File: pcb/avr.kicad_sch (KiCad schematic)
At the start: 17 parts, among them J11 PEN, J14 ATMegaSpare, J16 ATUART, J18 Reset ext, J4 AVR ISP, J6 Enable load, SW2 Reset btn, U22 ATmega128L-8A, Y3 16MHz

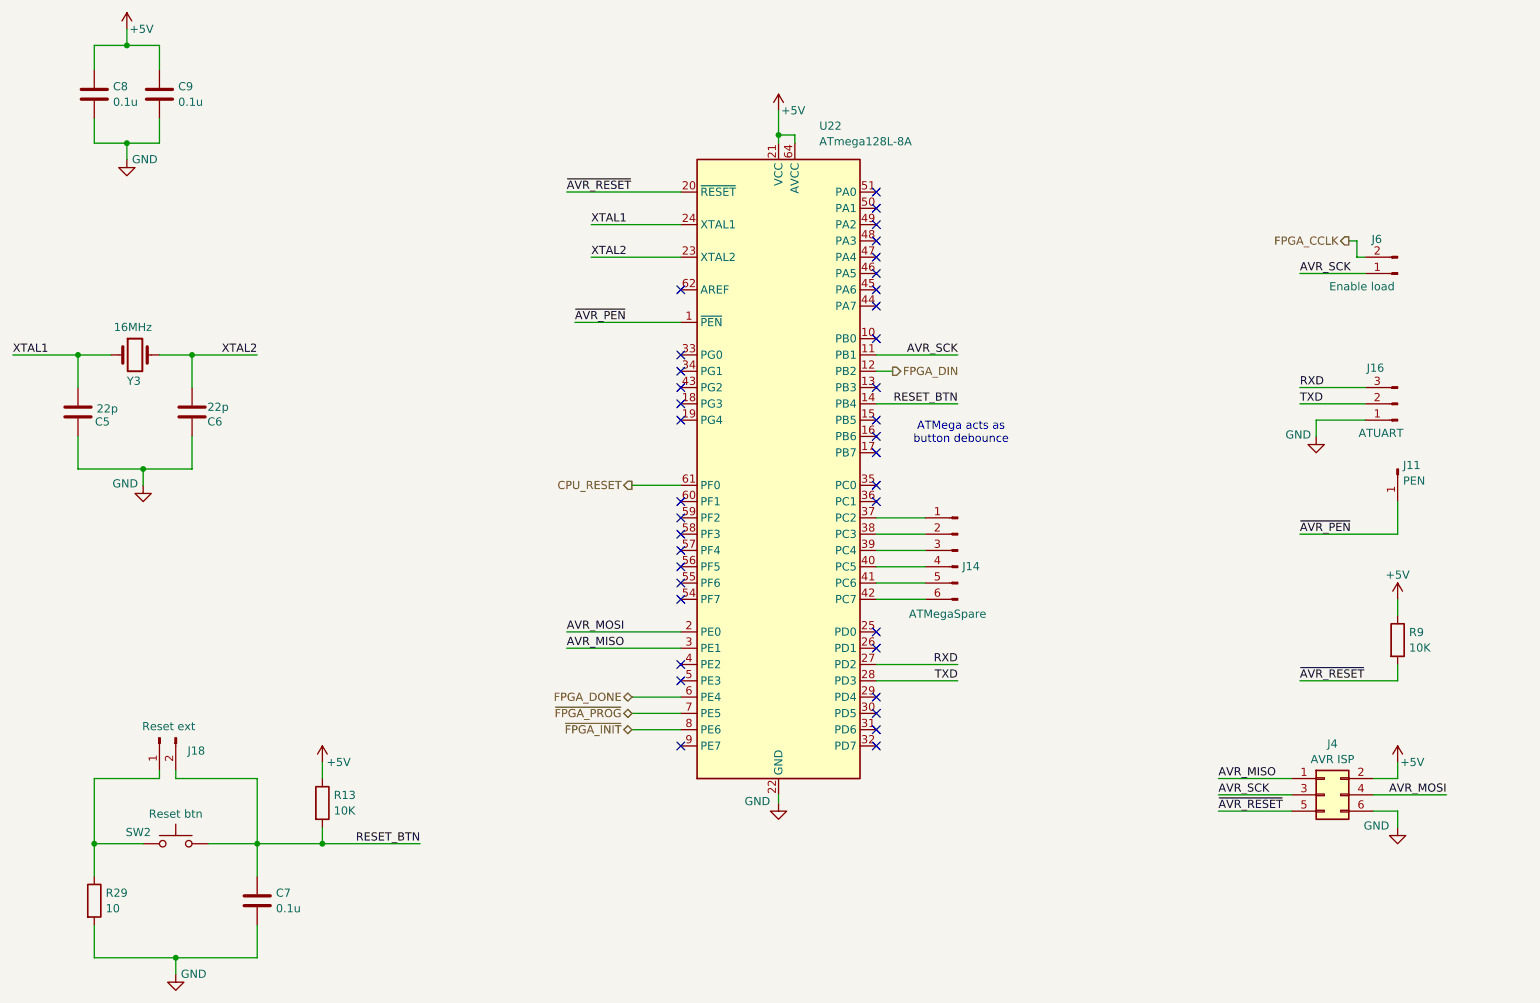
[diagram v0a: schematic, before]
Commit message: reshuffling atmega IO for better PCB routing
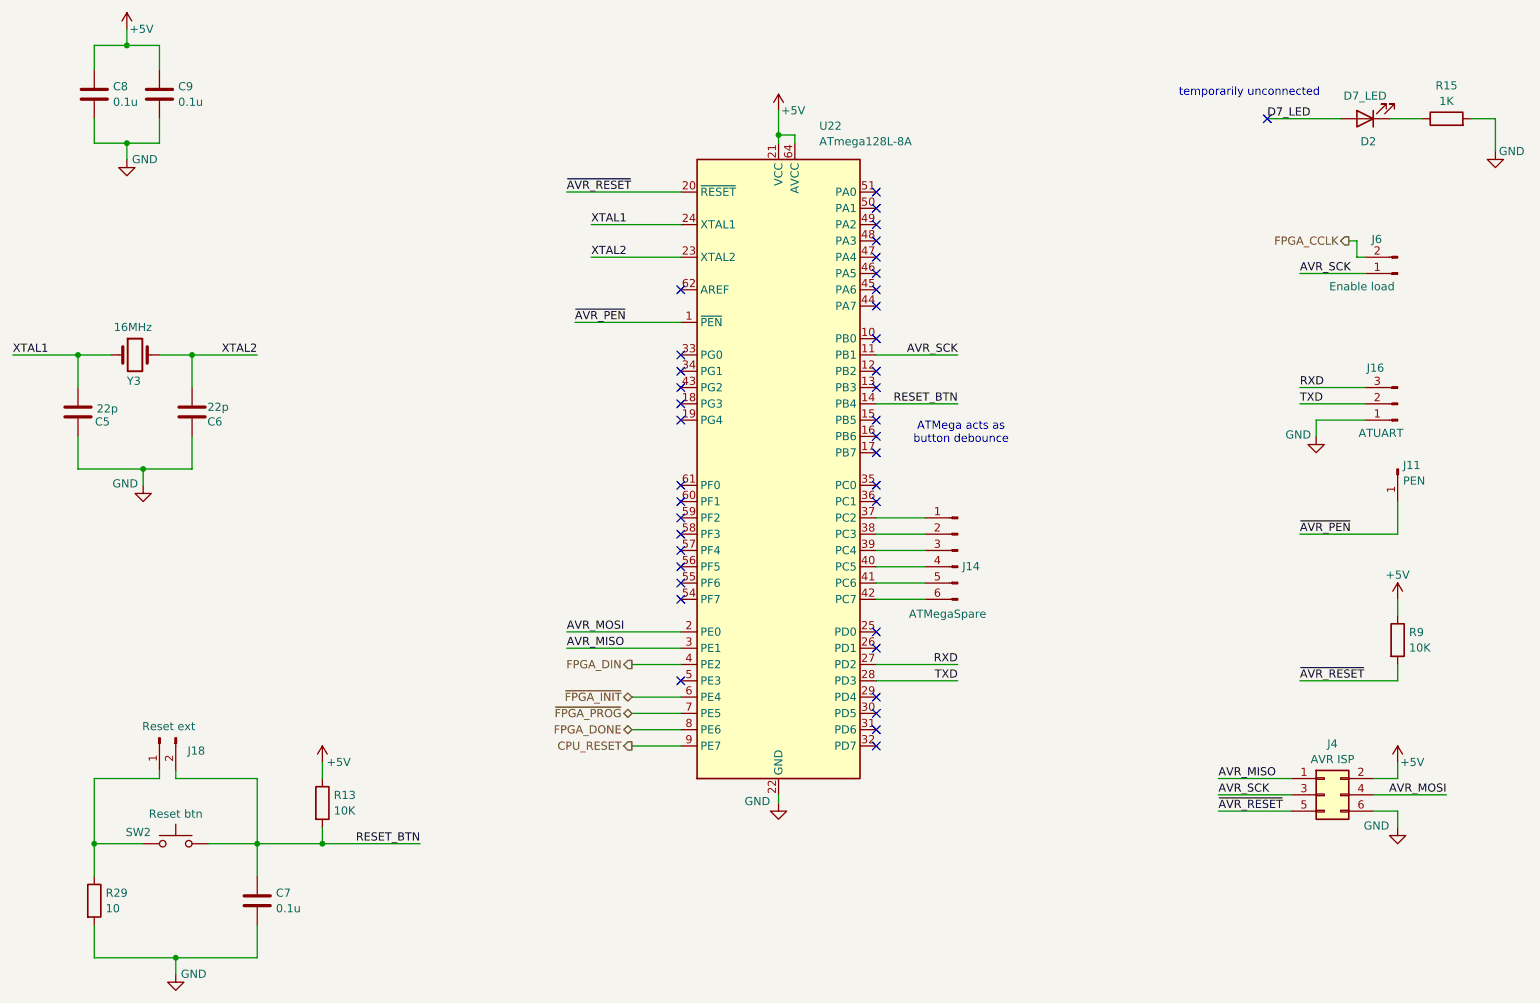
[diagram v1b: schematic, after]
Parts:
- added D2: D7_LED, LED_THT:LED_D4.0mm, symbol Device:LED
- added R15: 1K, Resistor_SMD:R_0805_2012Metric_Pad1.20x1.40mm_HandSolder, symbol Device:R
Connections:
- net CPU_RESET: now also U22.9 (PE7); no longer U22.61 (PF0)
- net FPGA_DIN: now also U22.4 (PE2); no longer U22.12 (PB2)
- net FPGA_DONE: now also U22.8 (PE6); no longer U22.6 (PE4)
- net GND: now also R15.2
- net ~{FPGA_INIT}: now also U22.6 (PE4); no longer U22.8 (PE6)
- new net: D2.1 (K), R15.1
- new net D7_LED: D2.2 (A)
- no-connect marks 37 -> 38
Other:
- note added: "temporarily unconnected"

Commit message: AVR diagram CMOS header, FPGA_DIN back to pin 12, CPU_RESET pin 5, simplified RESET_BTN circuit (pullup and debounce is inside AVR already)
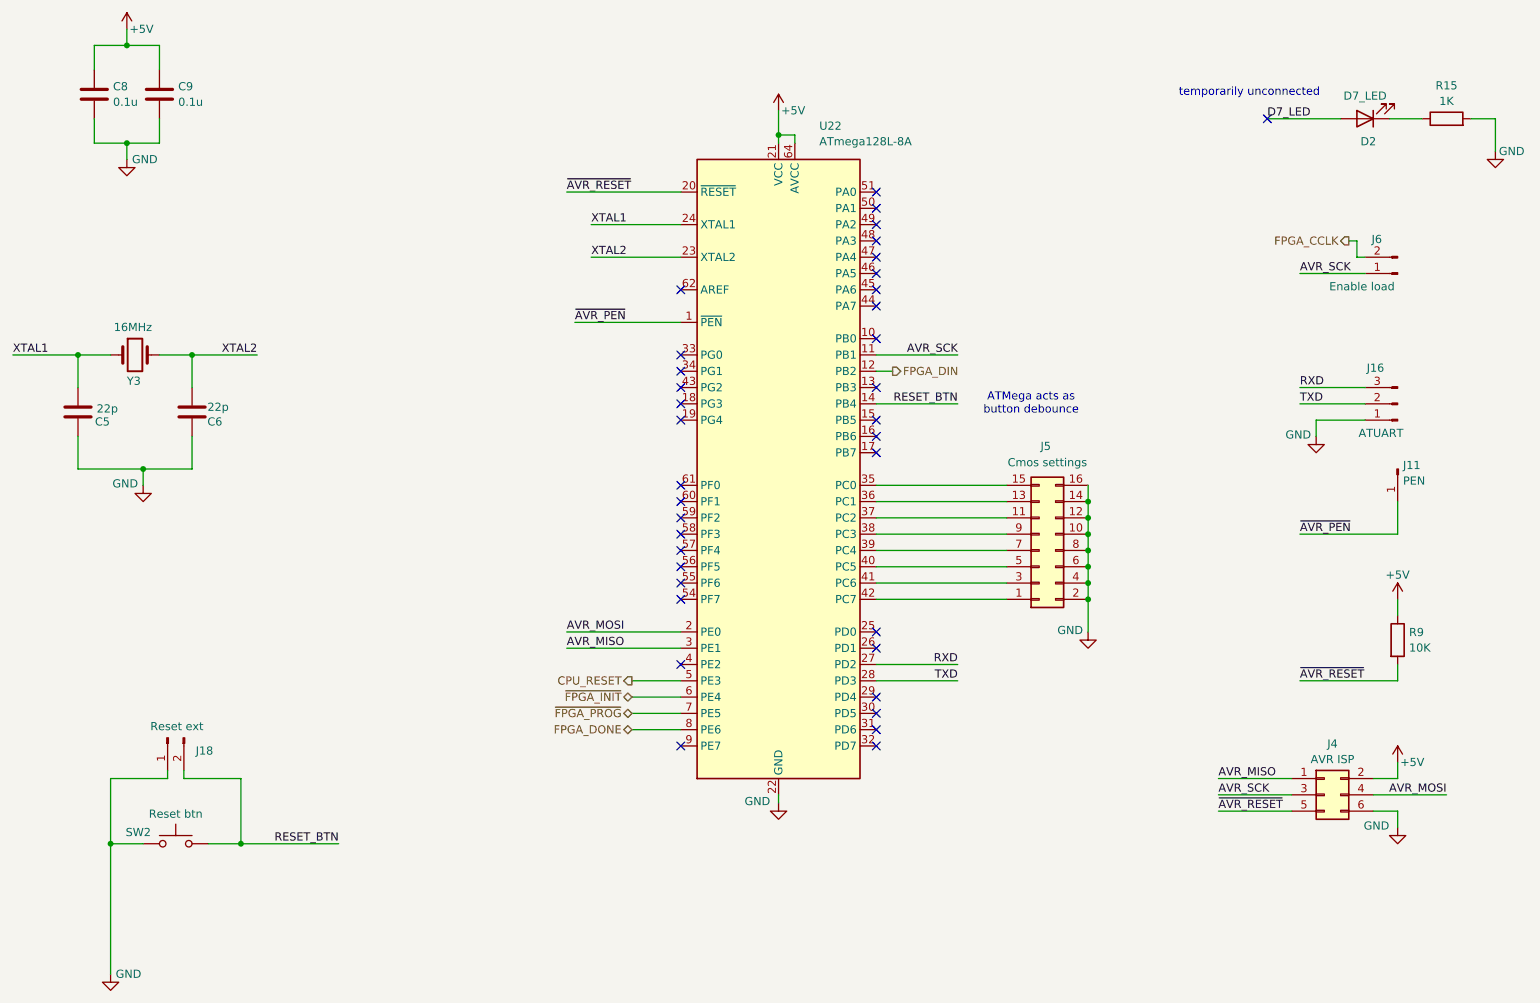
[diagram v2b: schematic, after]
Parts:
- removed C7: 0.1u, Capacitor_SMD:C_0805_2012Metric_Pad1.18x1.45mm_HandSolder, symbol Device:C
- removed J14: ATMegaSpare, Connector_PinHeader_2.54mm:PinHeader_1x06_P2.54mm_Vertical, symbol Connector:Conn_01x06_Pin
- removed R13: 10K, Resistor_SMD:R_0805_2012Metric_Pad1.20x1.40mm_HandSolder, symbol Device:R
- removed R29: 10, Resistor_SMD:R_0805_2012Metric_Pad1.20x1.40mm_HandSolder, symbol Device:R
- added J5: Cmos settings, Connector_PinHeader_2.54mm:PinHeader_2x08_P2.54mm_Vertical, symbol Connector_Generic:Conn_02x08_Odd_Even
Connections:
- net CPU_RESET: now also U22.5 (PE3); no longer U22.9 (PE7)
- net FPGA_DIN: now also U22.12 (PB2); no longer U22.4 (PE2)
- net GND: now also J18.1 (Pin_1), SW2.1, J5.10 (Pin_10), J5.12 (Pin_12), J5.14 (Pin_14), J5.16 (Pin_16), J5.2 (Pin_2), J5.4 (Pin_4), J5.6 (Pin_6), J5.8 (Pin_8)
- net at U22.37 (PC2): now also J5.11 (Pin_11)
- net at U22.38 (PC3): now also J5.9 (Pin_9)
- net at U22.39 (PC4): now also J5.7 (Pin_7)
- net at U22.40 (PC5): now also J5.5 (Pin_5)
- net at U22.41 (PC6): now also J5.3 (Pin_3)
- net at U22.42 (PC7): now also J5.1 (Pin_1)
- net at U22.35 (PC0): now also J5.15 (Pin_15)
- net at U22.36 (PC1): now also J5.13 (Pin_13)
- no-connect marks 38 -> 36
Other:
- moved on the sheet: J18

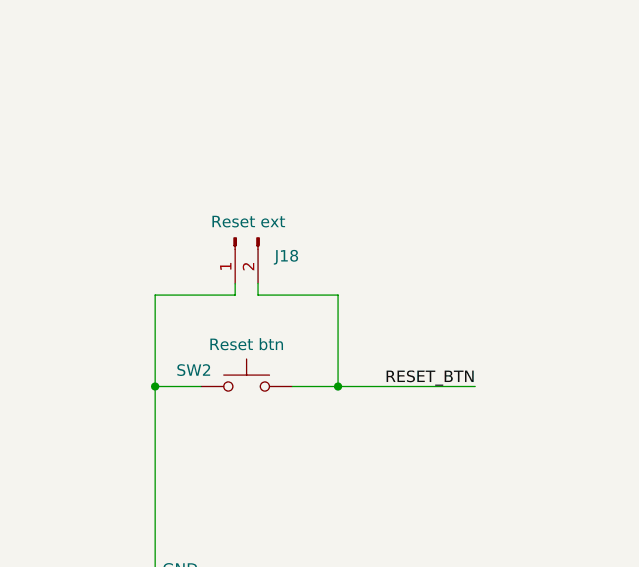
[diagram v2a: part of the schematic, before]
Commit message: AVR reset labels
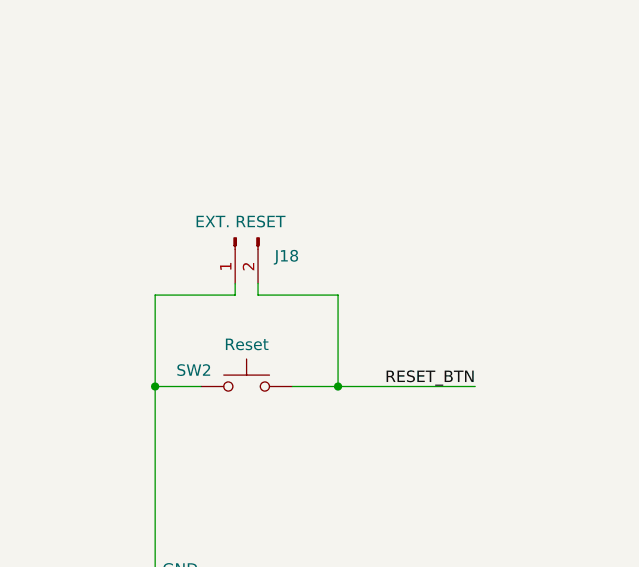
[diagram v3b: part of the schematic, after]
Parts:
- J18: value Reset ext -> EXT. RESET
- SW2: value Reset btn -> Reset
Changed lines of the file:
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@@
 			)
 		)
-		(property "Value" "Reset ext"
+		(property "Value" "EXT. RESET"
 			(at 52.578 131.572 90)
 			(effects
@@
 			)
 		)
-		(property "Value" "Reset btn"
+		(property "Value" "Reset"
 			(at 48.26 145.2188 0)
 			(effects
